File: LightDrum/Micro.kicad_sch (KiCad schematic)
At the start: 21 parts, among them J902 JTAG, Q901 RQ5A030AP, SW901 BOOT1, SW902 BOOT0, U901 24LC04, Y901 16MHz

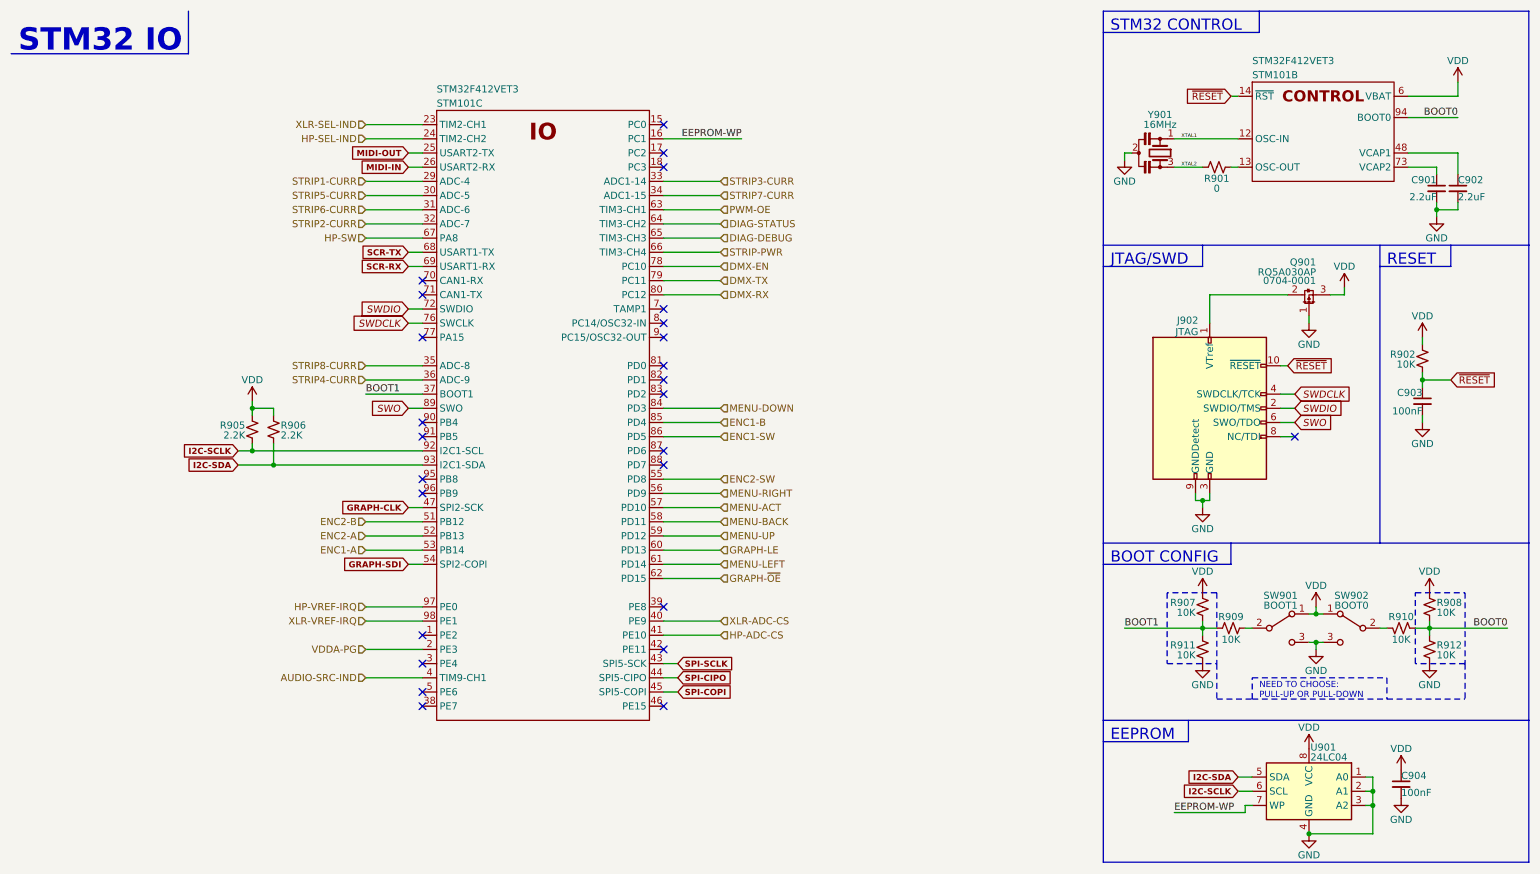
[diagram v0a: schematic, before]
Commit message: Start REV 10 - Fix small issues
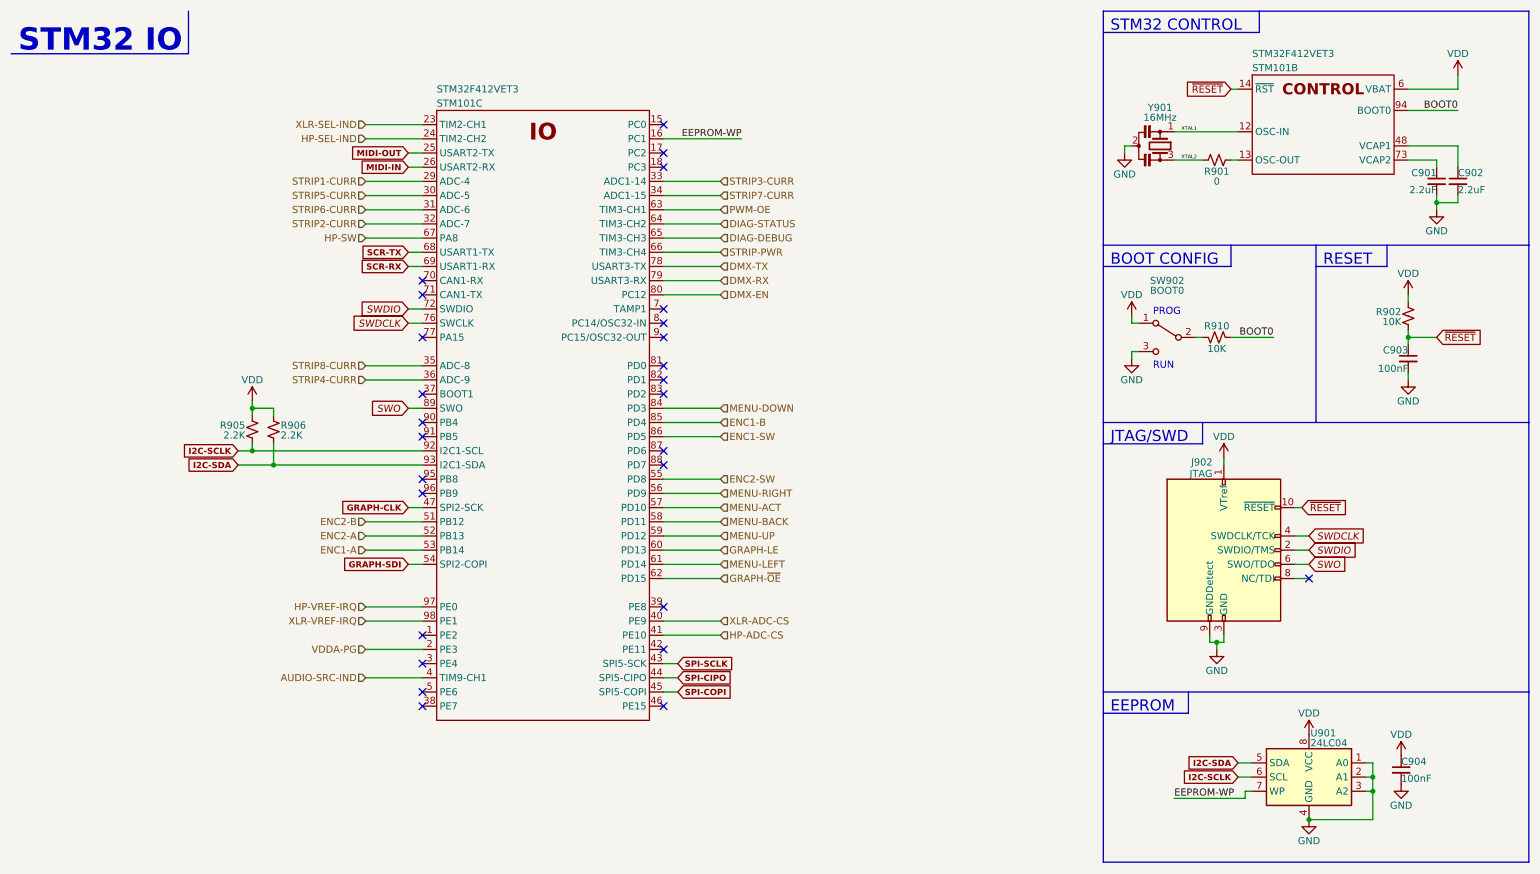
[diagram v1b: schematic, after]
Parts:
- removed Q901: RQ5A030AP, Package_TO_SOT_SMD:SOT-23, symbol Daxxn_Transistors:RQ5A030AP
- removed R907, R908, R909, R911, R912: 10K, Resistor_SMD:R_0402_1005Metric, symbol Device:R_Small_US
- removed SW901: BOOT1, Daxxn_Switches:PCM12SMTR, symbol Switch:SW_SPDT
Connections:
- net DMX-EN: now also STM101.80 (PC12); no longer STM101.78 (PC10)
- net DMX-RX: now also STM101.79 (PC11); no longer STM101.80 (PC12)
- net DMX-TX: now also STM101.78 (PC10); no longer STM101.79 (PC11)
- net VDD: now also J902.1 (VTref)
- net BOOT1: no longer names the net of STM101.37 (PB2)
- no-connect marks 26 -> 27
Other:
- note added: "PROG"
- note added: "RUN"
- note removed: "NEED TO CHOOSE: PULL-UP OR PULL-DOWN"
- moved on the sheet: C901, C902, C903, C904, J902, R901, R902, R910, STM101B, SW902, U901, Y901
